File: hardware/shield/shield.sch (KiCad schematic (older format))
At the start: 41 parts, among them J10 10118193-0001LF, SW1 RESET, U1 LM1117, U2 74LV4052, U3 TXB0104, Y1 12M

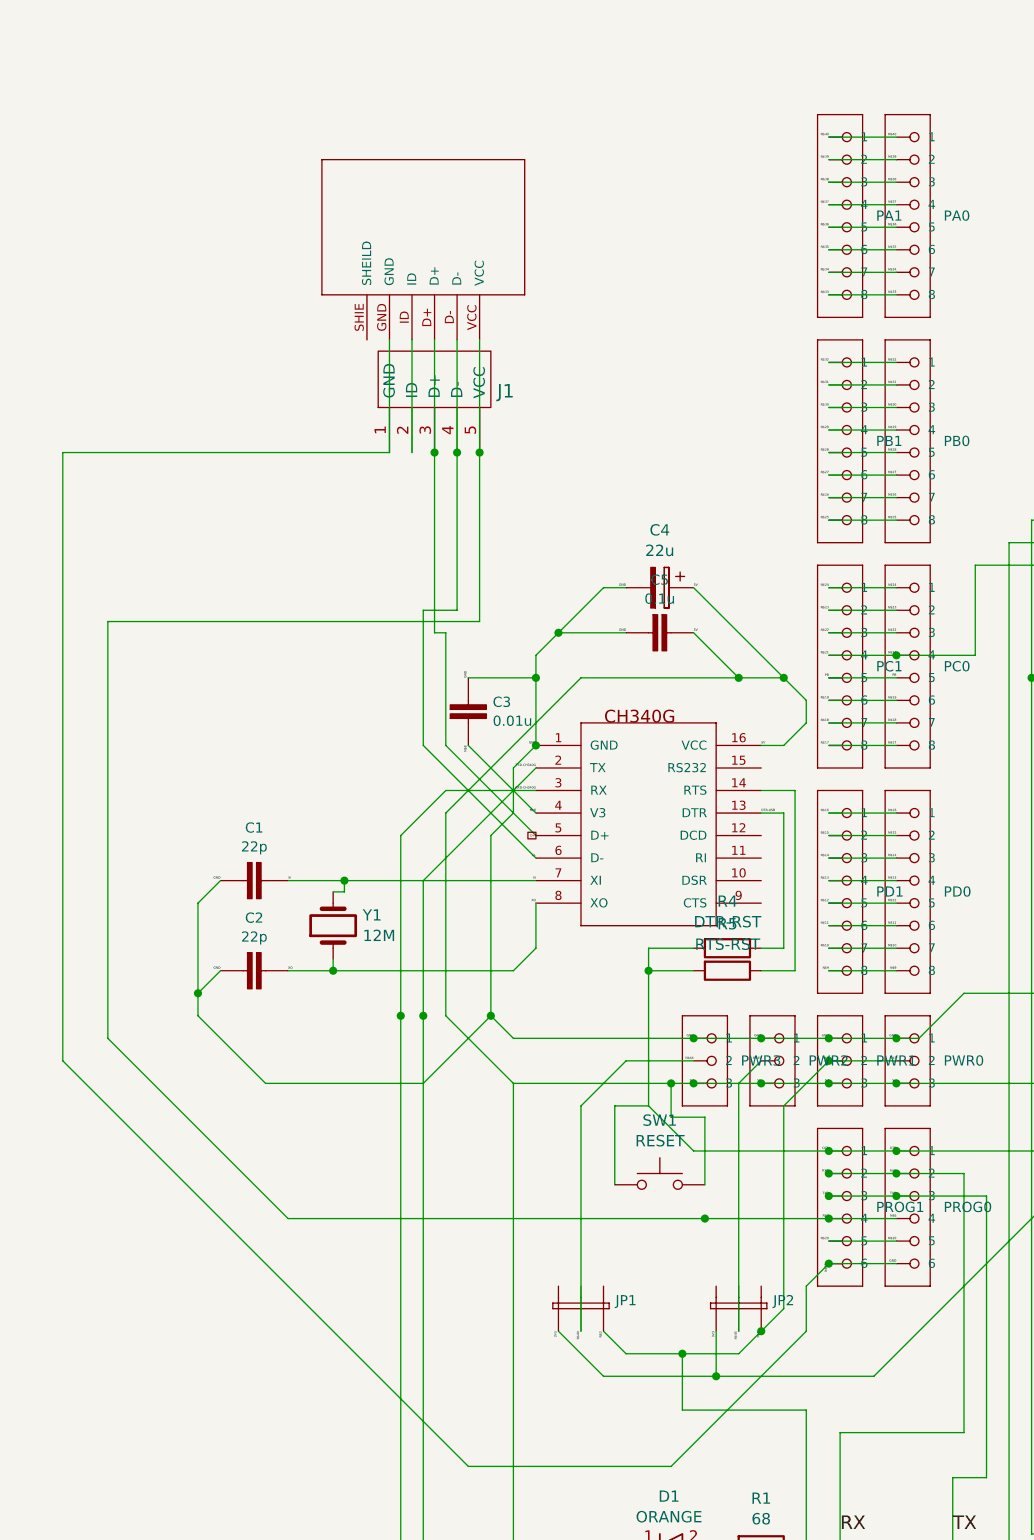
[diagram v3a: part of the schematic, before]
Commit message: Fully working; switched to USB MINI B.
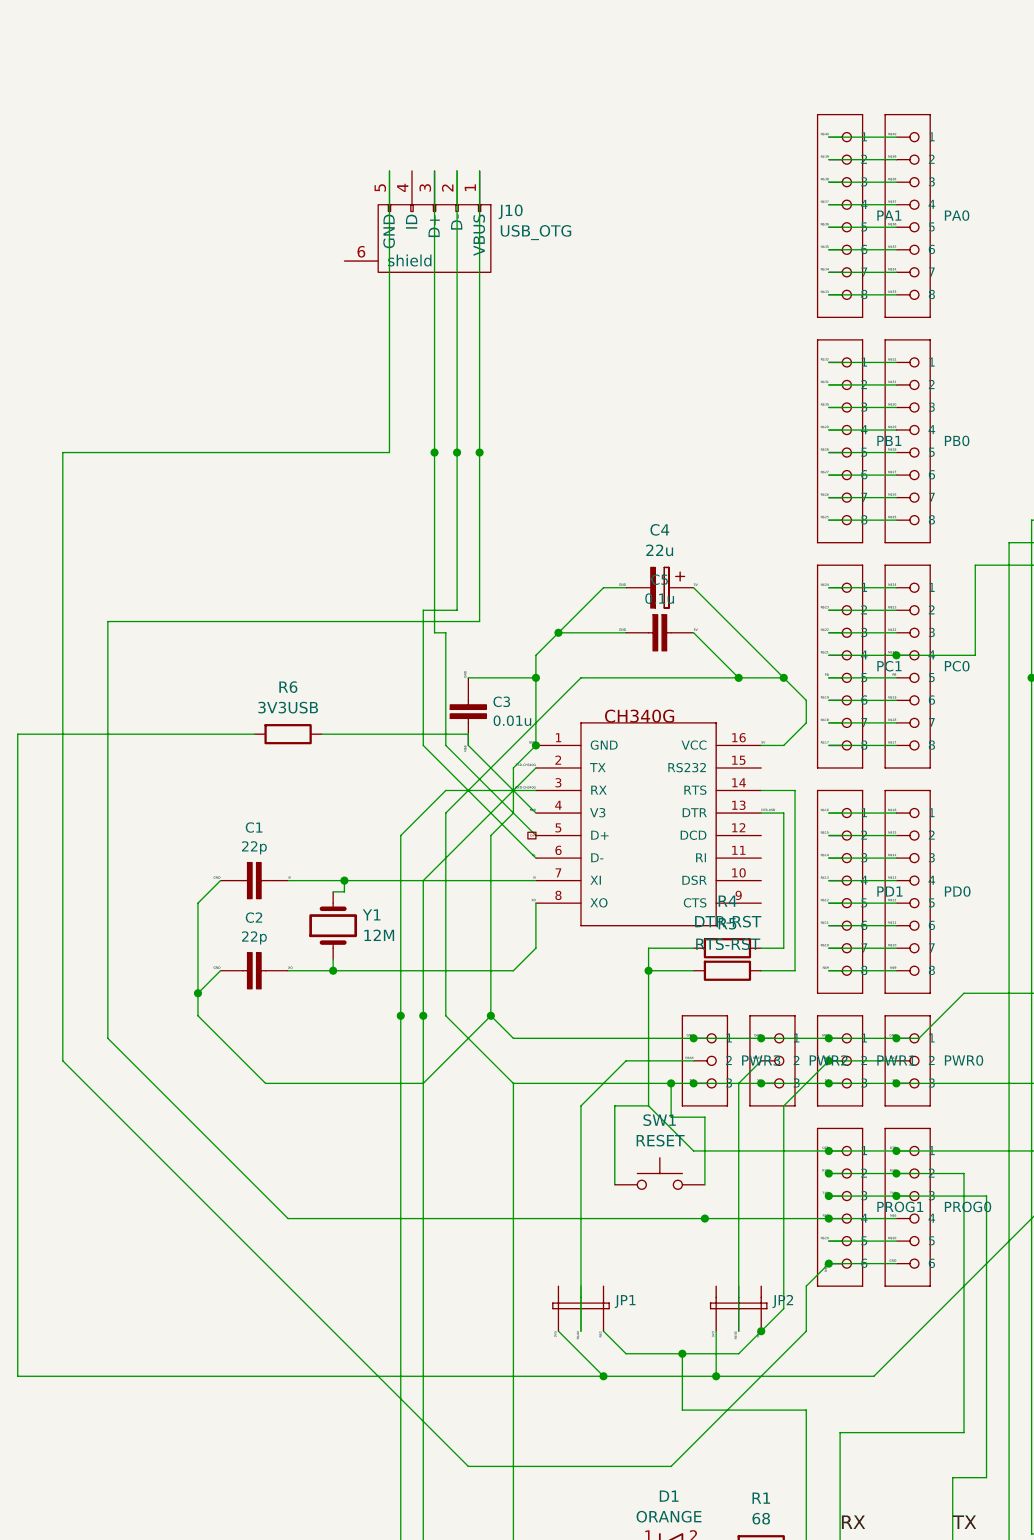
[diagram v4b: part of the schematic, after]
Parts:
- removed J1: ~, Pin_Headers:Pin_Header_Straight_1x05, symbol USBStandoff
- removed J10: 10118193-0001LF, shield:10118193-0001LF_10118193-0001LF, symbol 10118193-0001LF_10118193-0001LF
- added J10: USB_OTG, shield-pretty:USB_Mini-B, symbol USB_OTG
- added R6: 3V3USB, Capacitors_SMD:C_0805, symbol R
- JP1, JP2: footprint shield:SPARKFUN-RETIRED_SJ_3 -> Pin_Headers:Pin_Header_Straight_1x03
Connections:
- net 3V3: now also R6.2
- net D+: now also J10.3 (D+)
- net D-: now also J10.2 (D-)
- net GND: now also J10.5 (GND)
- net N$6: now also J10.1 (VBUS)
- net N$8: now also R6.1
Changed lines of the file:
@@
 $EndDescr
-$Comp
-L 10118193-0001LF_10118193-0001LF J10
-U 1 1 58543665
-P 8950 5250
-F 0 "J10" H 8940 5240 65  0001 L TNN
-F 1 "10118193-0001LF" H 8940 5140 65  0001 L TNN
-F 2 "shield:10118193-0001LF_10118193-0001LF" H 8940 5040 65  0001 L TNN
-F 3 "" H 8950 5250 60  0001 C CNN
-	1    8950 5250
-	0    1    1    0
-$EndComp
 $Comp
 L CH340G_CH340G U$1
@@
 F 0 "JP1" H 9753 9986 45  0000 L CNN
 F 1 "~" H 9753 9902 45  0000 L CNN
-F 2 "shield:SPARKFUN-RETIRED_SJ_3" H 9500 9950 60  0001 C CNN
+F 2 "Pin_Headers:Pin_Header_Straight_1x03" H 9500 9950 60  0001 C CNN
 F 3 "" H 9500 9950 60  0001 C CNN
 	1    9500 9950
@@
 F 0 "JP2" H 10453 9986 45  0000 L CNN
 F 1 "~" H 10453 9902 45  0000 L CNN
-F 2 "shield:SPARKFUN-RETIRED_SJ_3" H 10200 9950 60  0001 C CNN
+F 2 "Pin_Headers:Pin_Header_Straight_1x03" H 10200 9950 60  0001 C CNN
 F 3 "" H 10200 9950 60  0001 C CNN
 	1    10200 9950
@@
 Connection ~ 9400 7450
 Wire Wire Line
-	9100 7150 9400 7150
-Wire Wire Line
 	12200 8050 11900 8050
 Wire Wire Line
@@
 	9700 10250 9500 10050
 Wire Wire Line
-	9700 10250 10900 10250
+	7100 10250 10900 10250
 Wire Wire Line
 	10900 10250 11800 9350
@@
 	11350 6650 14850 6650
 Connection ~ 11000 7050
-$Comp
-L USBStandoff J1
-U 1 1 585C9231
-P 9050 5950
-F 0 "J1" V 9122 5772 60  0000 R CNN
-F 1 "~" V 9016 5772 60  0000 R CNN
-F 2 "Pin_Headers:Pin_Header_Straight_1x05" H 9050 5950 60  0001 C CNN
-F 3 "" H 9050 5950 60  0001 C CNN
-	1    9050 5950
-	0    -1   -1   0
-$EndComp
 Wire Wire Line
 	9150 6900 7500 6900
 Wire Wire Line
-	9150 5650 9150 6900
-Wire Wire Line
-	7300 6150 8750 6150
+	9150 4900 9150 6900
+Wire Wire Line
+	8750 6150 7300 6150
 Wire Wire Line
 	9000 6950 9000 7450
@@
 	8950 6950 9000 6950
 Wire Wire Line
-	8950 5650 8950 6950
+	8950 4900 8950 6950
 Wire Wire Line
 	8900 7450 8900 6850
@@
 	8900 6850 9050 6850
 Wire Wire Line
-	9050 6850 9050 5650
-Wire Wire Line
-	8750 6150 8750 5650
-Wire Wire Line
-	8850 6150 8850 5650
+	9050 6850 9050 4900
+Wire Wire Line
+	8750 4900 8750 6150
 Connection ~ 8950 6150
 Connection ~ 9050 6150
@@
 	10150 9100 10150 9400
 Connection ~ 10000 8950
+$Comp
+L USB_OTG J10
+U 1 1 585DAE93
+P 8950 5200
+F 0 "J10" H 8662 5077 50  0000 R CNN
+F 1 "USB_OTG" H 8662 5168 50  0000 R CNN
+F 2 "shield-pretty:USB_Mini-B" V 8900 5100 50  0001 C CNN
+F 3 "" V 8900 5100 50  0000 C CNN
+	1    8950 5200
+	-1   0    0    1
+$EndComp
+Wire Wire Line
+	9100 7150 9400 7150
+Wire Wire Line
+	9100 7450 9100 7400
+Wire Wire Line
+	7100 7400 7100 10250
+Connection ~ 9700 10250
+$Comp
+L R R6
+U 1 1 585DD6EF
+P 8300 7400
+F 0 "R6" V 8093 7400 50  0000 C CNN
+F 1 "3V3USB" V 8184 7400 50  0000 C CNN
+F 2 "Capacitors_SMD:C_0805" V 8230 7400 50  0001 C CNN
+F 3 "" H 8300 7400 50  0000 C CNN
+	1    8300 7400
+	0    1    1    0
+$EndComp
+Wire Wire Line
+	9100 7400 8450 7400
+Wire Wire Line
+	8150 7400 7100 7400
 $EndSCHEMATC
